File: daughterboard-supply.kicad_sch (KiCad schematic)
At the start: 19 parts, among them J9 39281103, SW1 1X03, U15 AP62301WU-7, U4 AP62301WU-7

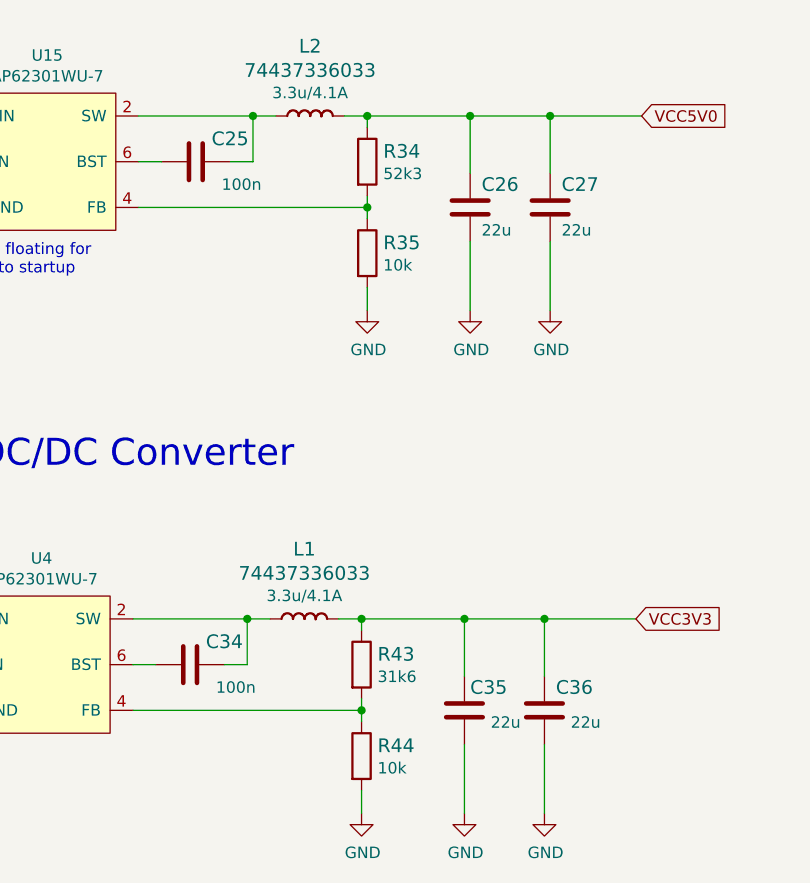
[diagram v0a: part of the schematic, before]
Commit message: R34,R35,R43,R44 on daughterboard updated
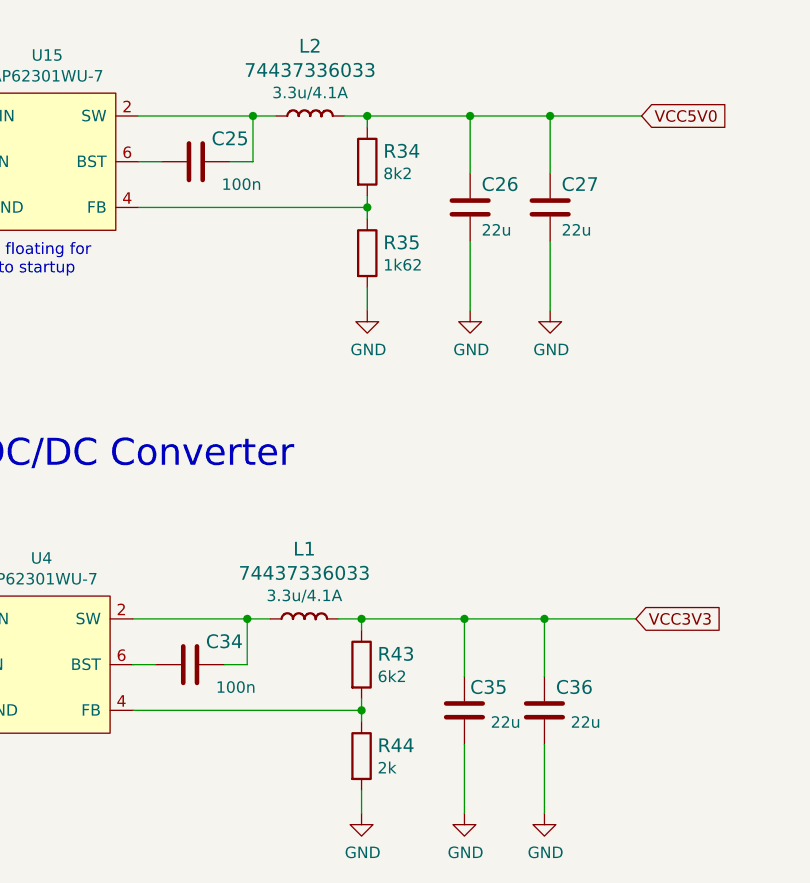
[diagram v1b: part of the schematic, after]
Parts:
- R34: value R_52k3_0402 -> R_8k2_0402; Val 52k3 -> 8k2
- R35: value R_10k_0402 -> R_1k62_0402; Val 10k -> 1k62
- R43: value R_31k6_0402 -> R_6k2_0402; Val 31k6 -> 6k2
- R44: value R_10k_0402 -> R_2k_0402; Val 10k -> 2k
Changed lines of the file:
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@@
       (effects (font (size 1.524 1.524)) (justify left))
     )
-    (property "Value" "R_10k_0402" (id 1) (at 178.435 128.905 0)
+    (property "Value" "R_1k62_0402" (id 1) (at 178.435 128.905 0)
       (effects (font (size 1.524 1.524)) hide)
     )
@@
       (effects (font (size 1.524 1.524)) (justify left) hide)
     )
-    (property "Val" "10k" (id 6) (at 184.023 130.2512 90)
+    (property "Val" "1k62" (id 6) (at 184.023 130.2512 90)
       (effects (font (size 1.27 1.27)) (justify left))
     )
@@
       (effects (font (size 1.524 1.524)) (justify left))
     )
-    (property "Value" "R_52k3_0402" (id 1) (at 178.435 118.745 0)
+    (property "Value" "R_8k2_0402" (id 1) (at 178.435 118.745 0)
       (effects (font (size 1.524 1.524)) hide)
     )
@@
       (effects (font (size 1.524 1.524)) (justify left) hide)
     )
-    (property "Val" "52k3" (id 6) (at 184.023 120.0912 90)
+    (property "Val" "8k2" (id 6) (at 184.023 120.0912 90)
       (effects (font (size 1.27 1.27)) (justify left))
     )
@@
       (effects (font (size 1.524 1.524)) (justify left))
     )
-    (property "Value" "R_31k6_0402" (id 1) (at 177.8 174.625 0)
+    (property "Value" "R_6k2_0402" (id 1) (at 177.8 174.625 0)
       (effects (font (size 1.524 1.524)) hide)
     )
@@
       (effects (font (size 1.524 1.524)) (justify left) hide)
     )
-    (property "Val" "31k6" (id 6) (at 183.388 175.9712 90)
+    (property "Val" "6k2" (id 6) (at 183.388 175.9712 90)
       (effects (font (size 1.27 1.27)) (justify left))
     )
@@
       (effects (font (size 1.524 1.524)) (justify left))
     )
-    (property "Value" "R_10k_0402" (id 1) (at 177.8 184.785 0)
+    (property "Value" "R_2k_0402" (id 1) (at 177.8 184.785 0)
       (effects (font (size 1.524 1.524)) hide)
     )
@@
       (effects (font (size 1.524 1.524)) (justify left) hide)
     )
-    (property "Val" "10k" (id 6) (at 183.388 186.1312 90)
-      (effects (font (size 1.27 1.27)) (justify left))
-    )
+    (property "Val" "2k" (id 6) (at 183.388 186.1312 90)
+      (effects (font (size 1.27 1.27)) (justify left))
+    )

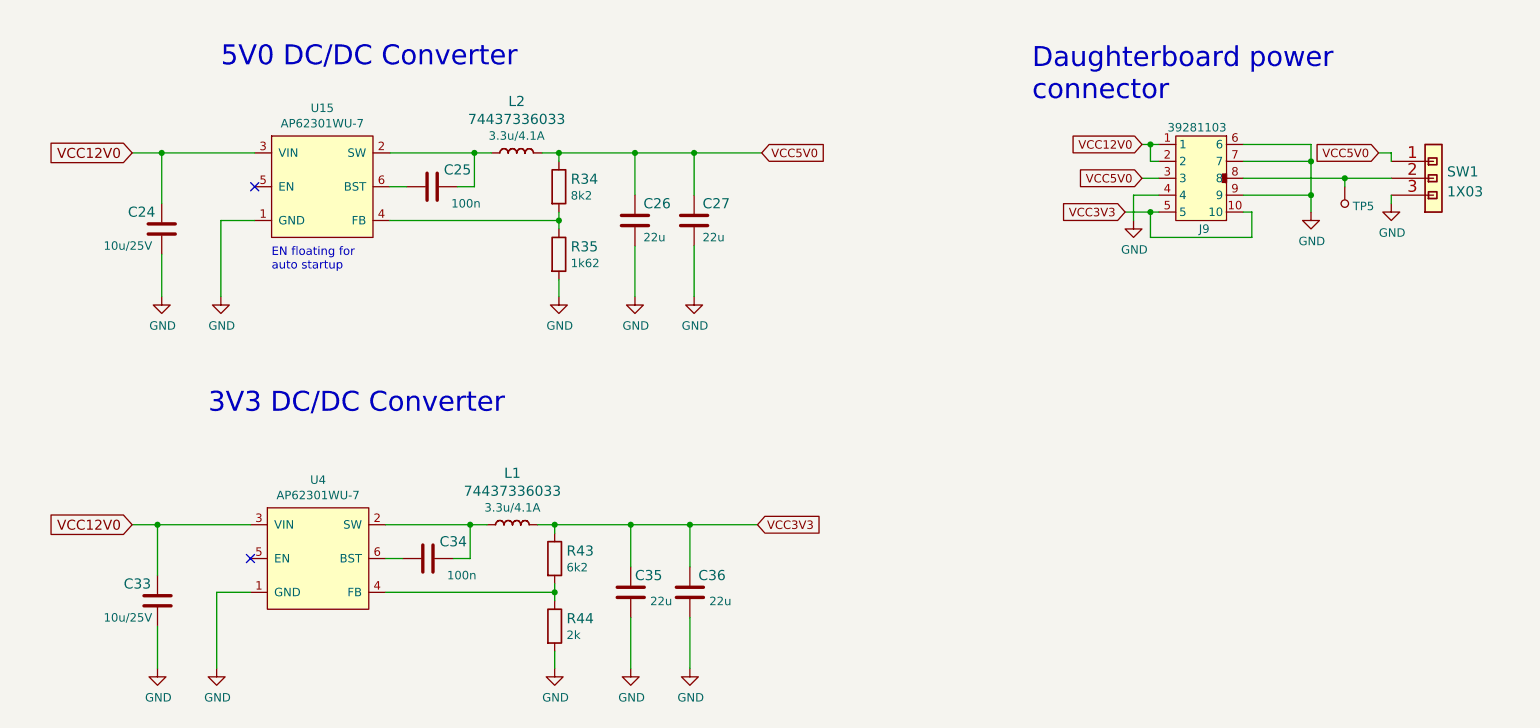
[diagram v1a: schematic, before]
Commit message: updated R34, R35, R43, R44
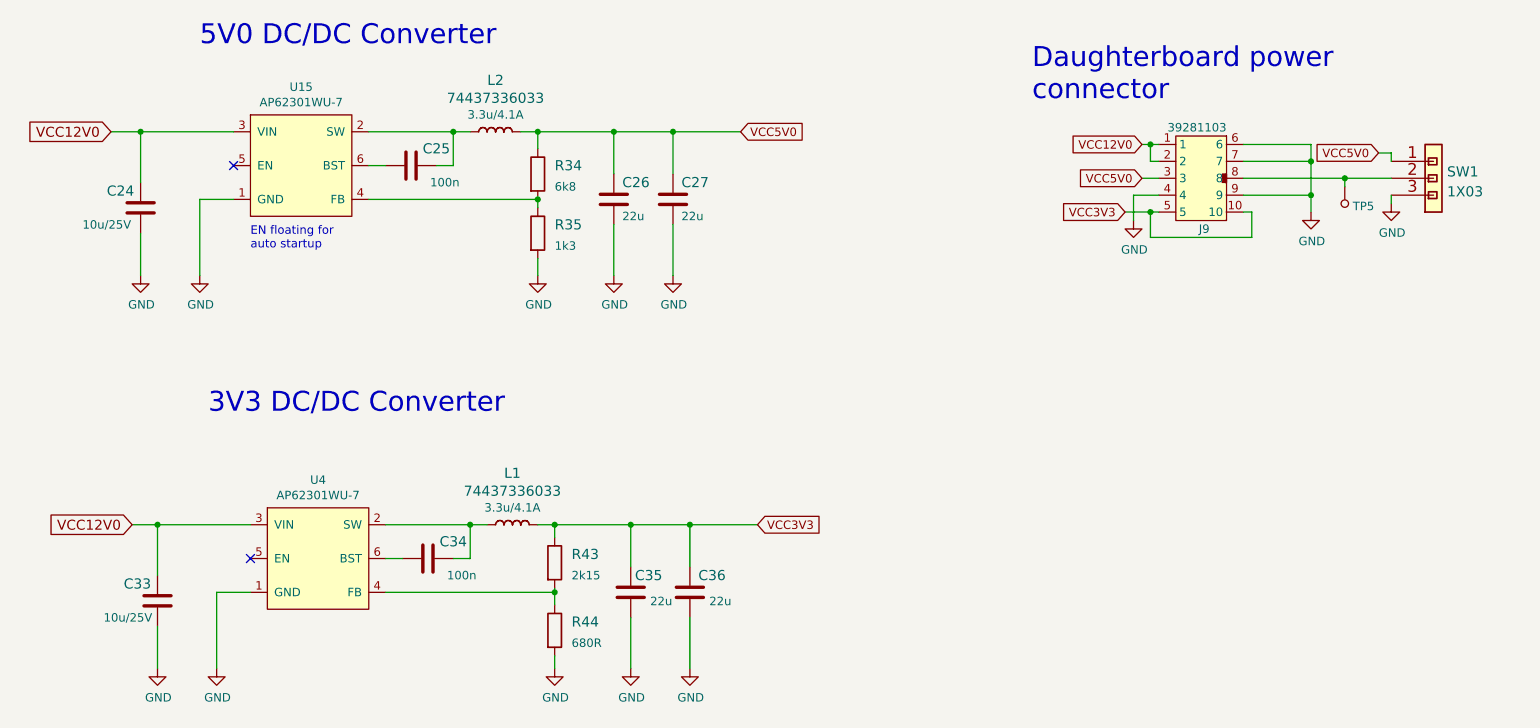
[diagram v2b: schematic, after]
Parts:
- removed R34: R_8k2_0402, d1600e-psu-breakout-board-footprints:0402-res, symbol d1600e-psu-breakout-board:R_52k3_0402
- removed R35: R_1k62_0402, d1600e-psu-breakout-board-footprints:0402-res, symbol d1600e-psu-breakout-board:R_10k_0402
- removed R43: R_6k2_0402, d1600e-psu-breakout-board-footprints:0402-res, symbol d1600e-psu-breakout-board:R_31k6_0402
- removed R44: R_2k_0402, d1600e-psu-breakout-board-footprints:0402-res, symbol d1600e-psu-breakout-board:R_10k_0402
- added R34: R_6k8_0402, antmicro-footprints:0402-res, symbol antmicroResistors0402:R_6k8_0402
- added R35: R_1k3_0402, antmicro-footprints:0402-res, symbol antmicroResistors0402:R_1k3_0402
- added R43: R_2k15_0402, antmicro-footprints:0402-res, symbol antmicroResistors0402:R_2k15_0402
- added R44: R_680R_0402, antmicro-footprints:0402-res, symbol antmicroResistors0402:R_680R_0402
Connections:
- net GND: now also R35.2, R44.2
- net VCC3V3: now also R43.1
- net VCC5V0: now also R34.1
- net at U15.4 (FB): now also R34.2, R35.1
- net at U4.4 (FB): now also R43.2, R44.1
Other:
- moved on the sheet: C24, C25, C26, C27, L2, U15

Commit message: [#63472] Add OHP assets
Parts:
- removed J9: 39281103, d1600e-psu-breakout-board-footprints:MOLEX_39281103, symbol d1600e-psu-breakout-board:39281103
- removed TP5: TP_SMD1MM, antmicro-footprints:Testpoint_smd_1mm, symbol antmicroTestPoints:TP_SMD1MM
- added J9: Molex_Mini-Fit-Jr_2x5_39-28-1103, antmicro-footprints:MOLEX_39281103, symbol antmicroWire2BoardConnectors:Molex_Mini-Fit-Jr_2x5_39-28-1103
- added TP5: TP_1mm_SMD, antmicro-footprints:TP_SMD_1mm, symbol antmicroTestPoints:TP_1mm_SMD
- C24, C33: value C_10u_16V_0603 -> C_10u_25V_0603; footprint d1600e-psu-breakout-board-footprints:0603-cap -> antmicro-footprints:C_0603_1608Metric; symbol d1600e-psu-breakout-board:C_10u_25V_0603 -> antmicroCapacitors0603:C_10u_25V_0603; Author (none) -> Antmicro; License (none) -> Apache-2.0; Val 10u/25V -> 10u; Voltage (none) -> 25V
- C25, C34: footprint d1600e-psu-breakout-board-footprints:0402-cap -> antmicro-footprints:C_0402_1005Metric; symbol d1600e-psu-breakout-board:C_100n_0402 -> antmicroCapacitors0402:C_100n_0402; Author (none) -> Antmicro; Dielectric (none) -> X5R; License (none) -> Apache-2.0; Voltage (none) -> 50V
- C26, C27, C35, C36: footprint d1600e-psu-breakout-board-footprints:0603-cap -> antmicro-footprints:C_0603_1608Metric; symbol d1600e-psu-breakout-board:C_22u_0603 -> antmicroCapacitors0603:C_22u_0603; Author (none) -> Antmicro; License (none) -> Apache-2.0; Manufacturer MURATA -> Murata
- L1, L2: value 74437336033 -> L_3u3_4.1A_WE-LHMI-5030; footprint d1600e-psu-breakout-board-footprints:WE_74437336033 -> antmicro-footprints:L_WE-LHMI-5030; symbol d1600e-psu-breakout-board:74437336033 -> antmicroFixedInductors:L_3u3_4.1A_WE-LHMI-5030; Author (none) -> Antmicro; IMax (none) -> 4.1A; ISat (none) -> 5.45A; License (none) -> Apache-2.0; Manufacturer Wurth Elektronik -> Würth Elektronik; MaxCur 4.1A -> (none); Val 3.3u/4.1A -> 3u3/4.1A
- R34: footprint antmicro-footprints:0402-res -> antmicro-footprints:R_0402_1005Metric; Author (none) -> Antmicro; License (none) -> Apache-2.0; MPN RC0402FR-076K8L -> CR0402-FX-6801GLF; Manufacturer YAGEO_(PHYCOMP) -> Bourns; Tolerance (none) -> 1%
- R35: footprint antmicro-footprints:0402-res -> antmicro-footprints:R_0402_1005Metric; Author (none) -> Antmicro; License (none) -> Apache-2.0; MPN CR0402-FX-1301GLF -> CR0402-FX-1301GLF; Tolerance (none) -> 1%
- R43: footprint antmicro-footprints:0402-res -> antmicro-footprints:R_0402_1005Metric; Author (none) -> Antmicro; License (none) -> Apache-2.0; MPN CRCW04022K00FKED -> CR0402-FX-2151GLF; Manufacturer VISHAY -> Bourns; Tolerance (none) -> 1%
- R44: footprint antmicro-footprints:0402-res -> antmicro-footprints:R_0402_1005Metric; Author (none) -> Antmicro; License (none) -> Apache-2.0; MPN 0402WGJ0681TCE -> CR0402-FX-6800GLF; Manufacturer ROYAL_OHM -> Bourns; Tolerance (none) -> 1%
- SW1: value 1X03 -> PinHeader_1x3_P2.54mm_Drill1.1mm; footprint antmicro-footprints:MH_1X03_2.54 -> antmicro-footprints:PinHeader_1x3_P2.54mm_Drill1.1mm; symbol antmicroRectangularConnectorsHeadersMalePins:1X03 -> antmicroGenericPinHeaders:PinHeader_1x3_P2.54mm_Drill1.1mm; Author (none) -> Antmicro; License (none) -> Apache-2.0; Manufacturer Wurth Elektronik -> Würth Elektronik
- U15, U4: value AP62301WU-7 -> AP62301_TSOT; footprint d1600e-psu-breakout-board-footprints:TSOT23-6 -> antmicro-footprints:TSOT23-6; symbol d1600e-psu-breakout-board:AP62301WU-7 -> antmicroDCDCConverters:AP62301_TSOT; Author (none) -> Antmicro; License (none) -> Apache-2.0
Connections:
- net GND: now also C24.1, C26.1, C27.1, C33.1, C35.1, C36.1, J9.4, J9.6, J9.7, J9.9; no longer C24.2, C26.2, C27.2, C33.2, C35.2, C36.2
- net VCC12V0: now also C24.2, C33.2, J9.1, J9.2; no longer C24.1, C33.1
- net VCC3V3: now also C35.2, C36.2, R43.2, J9.10, J9.5; no longer C35.1, C36.1, R43.1
- net VCC5V0: now also C26.2, C27.2, J9.3; no longer C26.1, C27.1
- net at L2.1, U15.2 (SW): now also C25.2; no longer C25.1
- net at U15.6 (BST): now also C25.1; no longer C25.2
- net at L1.1, U4.2 (SW): now also C34.2; no longer C34.1
- net at R44.1, U4.4 (FB): now also R43.1; no longer R43.2
- net at U4.6 (BST): now also C34.1; no longer C34.2
- net at SW1.2: now also J9.8, TP5.1
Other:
- moved on the sheet: C24, C25, C26, C27, C33, C34, C35, C36, R34, R35, R43, R44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
